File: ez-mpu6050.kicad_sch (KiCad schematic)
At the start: 25 parts, among them J1 I2C, J3 Conn_01x06, J4 Conn_01x06, J5 I2C, U1 MPU-6050, U2 AP2112K-3.3

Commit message: Finish tracks add zone & GND vias
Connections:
- net +3V3: now also J4.2 (Pin_2); no longer J3.2 (Pin_2)
- net AD0: now also J3.1 (Pin_1); no longer J4.1 (Pin_1)
- net CLKIN: now also J3.5 (Pin_5); no longer J4.5 (Pin_5)
- net FSYNC_IN: now also J3.2 (Pin_2); no longer J4.2 (Pin_2)
- net GND: now also J3.6 (Pin_6), J4.3 (Pin_3); no longer J3.3 (Pin_3), J4.6 (Pin_6)
- net INT: now also J4.6 (Pin_6); no longer J3.6 (Pin_6)
- net SCL: now also J4.4 (Pin_4); no longer J3.4 (Pin_4)
- net SCL_EXT: now also J3.3 (Pin_3); no longer J4.3 (Pin_3)
- net SDA: now also J4.5 (Pin_5); no longer J3.5 (Pin_5)
- net SDA_EXT: now also J3.4 (Pin_4); no longer J4.4 (Pin_4)
- net VDD: now also J4.1 (Pin_1); no longer J3.1 (Pin_1)
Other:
- moved on the sheet: J3, J4
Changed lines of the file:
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@@
     )
   )
-  (symbol (lib_id "Connector_Generic:Conn_01x06") (at 33.02 85.09 0) (mirror y) (unit 1)
+  (symbol (lib_id "Connector_Generic:Conn_01x06") (at 33.02 114.3 0) (mirror y) (unit 1)
     (in_bom yes) (on_board yes) (dnp no)
-    (property "Reference" "J3" (at 30.48 85.09 0)
-      (effects (font (size 1.27 1.27)) (justify left))
-    )
-    (property "Value" "Conn_01x06" (at 30.48 87.63 0)
-      (effects (font (size 1.27 1.27)) (justify left))
-    )
-    (property "Footprint" "Connector_PinHeader_2.54mm:PinHeader_1x06_P2.54mm_Vertical" (at 33.02 85.09 0)
-      (effects (font (size 1.27 1.27)) hide)
-    )
-    (property "Datasheet" "~" (at 33.02 85.09 0)
+    (property "Reference" "J3" (at 30.48 114.3 0)
+      (effects (font (size 1.27 1.27)) (justify left))
+    )
+    (property "Value" "Conn_01x06" (at 30.48 116.84 0)
+      (effects (font (size 1.27 1.27)) (justify left))
+    )
+    (property "Footprint" "Connector_PinHeader_2.54mm:PinHeader_1x06_P2.54mm_Vertical" (at 33.02 114.3 0)
+      (effects (font (size 1.27 1.27)) hide)
+    )
+    (property "Datasheet" "~" (at 33.02 114.3 0)
       (effects (font (size 1.27 1.27)) hide)
     )
@@
     )
   )
-  (symbol (lib_id "Connector_Generic:Conn_01x06") (at 33.02 114.3 0) (mirror y) (unit 1)
+  (symbol (lib_id "Connector_Generic:Conn_01x06") (at 33.02 85.09 0) (mirror y) (unit 1)
     (in_bom yes) (on_board yes) (dnp no)
-    (property "Reference" "J4" (at 30.48 114.3 0)
-      (effects (font (size 1.27 1.27)) (justify left))
-    )
-    (property "Value" "Conn_01x06" (at 30.48 116.84 0)
-      (effects (font (size 1.27 1.27)) (justify left))
-    )
-    (property "Footprint" "Connector_PinHeader_2.54mm:PinHeader_1x06_P2.54mm_Vertical" (at 33.02 114.3 0)
-      (effects (font (size 1.27 1.27)) hide)
-    )
-    (property "Datasheet" "~" (at 33.02 114.3 0)
-      (effects (font (size 1.27 1.27)) hide)
-    )
+    (property "Reference" "J4" (at 30.48 85.09 0)
+      (effects (font (size 1.27 1.27)) (justify left))
+    )
+    (property "Value" "Conn_01x06" (at 30.48 87.63 0)
+      (effects (font (size 1.27 1.27)) (justify left))
+    )
+    (property "Footprint" "Connector_PinHeader_2.54mm:PinHeader_1x06_P2.54mm_Vertical" (at 33.02 85.09 0)
+      (effects (font (size 1.27 1.27)) hide)
+    )
+    (property "Datasheet" "~" (at 33.02 85.09 0)
+      (effects (font (size 1.27 1.27)) hide)
+    )

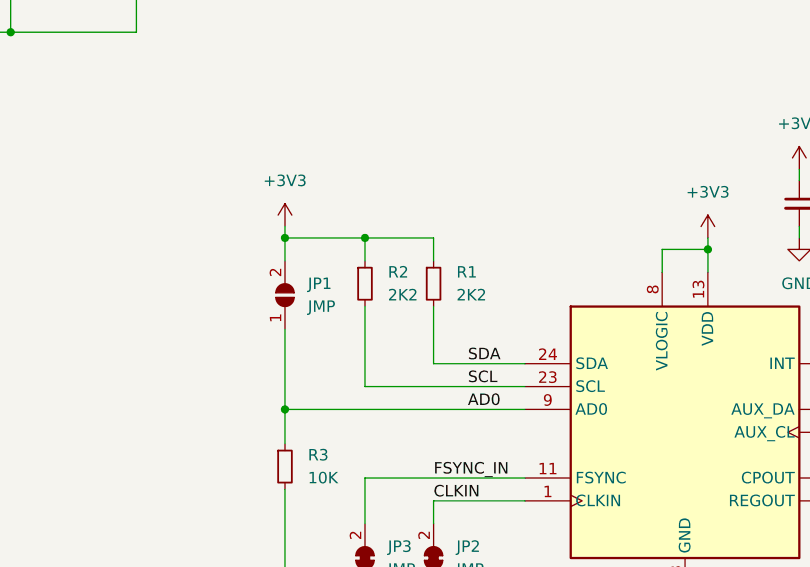
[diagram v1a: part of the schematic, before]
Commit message: Add RPU enable jumper
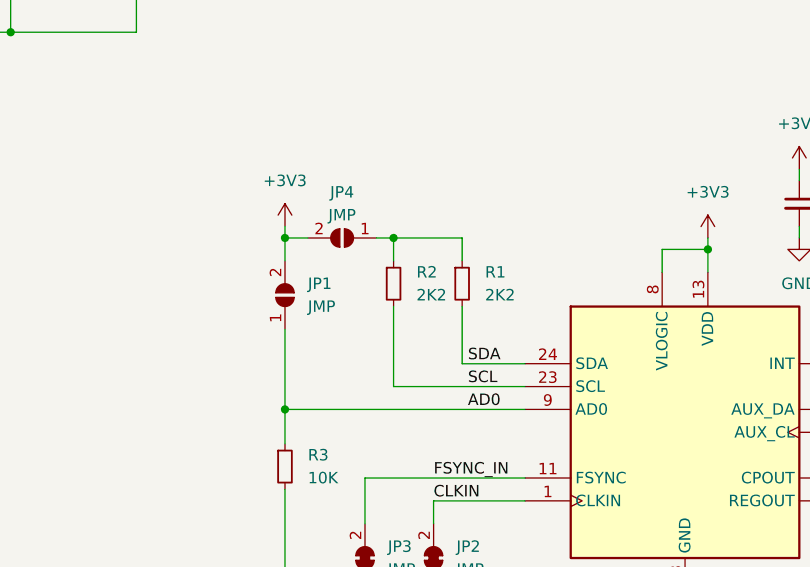
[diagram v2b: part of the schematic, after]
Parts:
- added JP4: JMP, Jumper:SolderJumper-2_P1.3mm_Open_RoundedPad1.0x1.5mm, symbol Jumper:SolderJumper_2_Open
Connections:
- net +3V3: now also JP4.2 (B); no longer R1.1, R2.1
- new net: JP4.1 (A), R1.1, R2.1
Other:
- moved on the sheet: R1, R2
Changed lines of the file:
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@@
   (junction (at 160.02 82.55) (diameter 0) (color 0 0 0 0)
   )
+  (junction (at 125.095 81.28) (diameter 0) (color 0 0 0 0)
+  )
   (junction (at 82.55 44.45) (diameter 0) (color 0 0 0 0)
   )
-  (junction (at 121.92 81.28) (diameter 0) (color 0 0 0 0)
-  )
   (junction (at 185.42 33.02) (diameter 0) (color 0 0 0 0)
   )
+  (junction (at 113.03 81.28) (diameter 0) (color 0 0 0 0)
+  )
   (junction (at 82.55 58.42) (diameter 0) (color 0 0 0 0)
   )
@@
   (junction (at 69.85 44.45) (diameter 0) (color 0 0 0 0)
   )
-  (junction (at 113.03 81.28) (diameter 0) (color 0 0 0 0)
-  )
   (junction (at 186.69 35.56) (diameter 0) (color 0 0 0 0)
   )
@@
     (stroke (width 0) (type default))
   )
-  (wire (pts (xy 121.92 97.79) (xy 139.7 97.79))
+  (wire (pts (xy 113.03 81.28) (xy 115.57 81.28))
+    (stroke (width 0) (type default))
+  )
+  (wire (pts (xy 125.095 97.79) (xy 139.7 97.79))
     (stroke (width 0) (type default))
   )
@@
     (stroke (width 0) (type default))
   )
-  (wire (pts (xy 121.92 81.28) (xy 129.54 81.28))
+  (wire (pts (xy 125.095 81.28) (xy 132.715 81.28))
     (stroke (width 0) (type default))
   )
@@
     (stroke (width 0) (type default))
   )
-  (wire (pts (xy 121.92 81.28) (xy 121.92 83.82))
+  (wire (pts (xy 125.095 81.28) (xy 125.095 83.82))
     (stroke (width 0) (type default))
   )
@@
     (stroke (width 0) (type default))
   )
+  (wire (pts (xy 113.03 81.28) (xy 113.03 83.82))
+    (stroke (width 0) (type default))
+  )
   (wire (pts (xy 154.94 85.09) (xy 154.94 82.55))
     (stroke (width 0) (type default))
@@
     (stroke (width 0) (type default))
   )
-  (wire (pts (xy 129.54 95.25) (xy 139.7 95.25))
+  (wire (pts (xy 132.715 95.25) (xy 139.7 95.25))
     (stroke (width 0) (type default))
   )
@@
     (stroke (width 0) (type default))
   )
-  (wire (pts (xy 113.03 81.28) (xy 121.92 81.28))
-    (stroke (width 0) (type default))
-  )
   (wire (pts (xy 38.1 119.38) (xy 48.26 119.38))
     (stroke (width 0) (type default))
@@
     (stroke (width 0) (type default))
   )
-  (wire (pts (xy 113.03 81.28) (xy 113.03 83.82))
-    (stroke (width 0) (type default))
-  )
   (wire (pts (xy 182.88 81.28) (xy 182.88 80.01))
     (stroke (width 0) (type default))
@@
     (stroke (width 0) (type default))
   )
-  (wire (pts (xy 129.54 88.9) (xy 129.54 95.25))
+  (wire (pts (xy 132.715 88.9) (xy 132.715 95.25))
     (stroke (width 0) (type default))
   )
@@
     (stroke (width 0) (type default))
   )
+  (wire (pts (xy 123.19 81.28) (xy 125.095 81.28))
+    (stroke (width 0) (type default))
+  )
   (wire (pts (xy 121.92 113.03) (xy 121.92 107.95))
     (stroke (width 0) (type default))
@@
     (stroke (width 0) (type default))
   )
-  (wire (pts (xy 121.92 88.9) (xy 121.92 97.79))
+  (wire (pts (xy 125.095 88.9) (xy 125.095 97.79))
     (stroke (width 0) (type default))
   )
@@
     (stroke (width 0) (type default))
   )
-  (wire (pts (xy 129.54 83.82) (xy 129.54 81.28))
+  (wire (pts (xy 132.715 83.82) (xy 132.715 81.28))
     (stroke (width 0) (type default))
   )
@@
       (effects (font (size 1.27 1.27)) hide)
     )
-    (pin "2")
-    (pin "1")
+    (pin "1")
+    (pin "2")
     (instances
       (project "ez-mpu6050"
@@
       (effects (font (size 1.27 1.27)) (justify bottom) hide)
     )
-    (pin "2")
+    (pin "1")
+    (pin "2")
+    (pin "3")
     (pin "4")
-    (pin "1")
     (pin "S1")
     (pin "S2")
-    (pin "3")
     (instances
       (project "ez-mpu6050"
@@
       (effects (font (size 1.27 1.27)) hide)
     )
-    (pin "6")
     (pin "1")
     (pin "2")
@@
     (pin "4")
     (pin "5")
+    (pin "6")
     (instances
       (project "ez-mpu6050"
@@
     )
   )
-  (symbol (lib_id "Device:R_Small") (at 129.54 86.36 0) (unit 1)
-    (in_bom yes) (on_board yes) (dnp no) (fields_autoplaced)
-    (property "Reference" "R1" (at 132.08 85.09 0)
-      (effects (font (size 1.27 1.27)) (justify left))
-    )
-    (property "Value" "2K2" (at 132.08 87.63 0)
-      (effects (font (size 1.27 1.27)) (justify left))
-    )
-    (property "Footprint" "Resistor_SMD:R_0402_1005Metric" (at 129.54 86.36 0)
-      (effects (font (size 1.27 1.27)) hide)
-    )
-    (property "Datasheet" "~" (at 129.54 86.36 0)
-      (effects (font (size 1.27 1.27)) hide)
-    )
-    (pin "2")
-    (pin "1")
+  (symbol (lib_id "Device:R_Small") (at 132.715 86.36 0) (unit 1)
+    (in_bom yes) (on_board yes) (dnp no) (fields_autoplaced)
+    (property "Reference" "R1" (at 135.255 85.09 0)
+      (effects (font (size 1.27 1.27)) (justify left))
+    )
+    (property "Value" "2K2" (at 135.255 87.63 0)
+      (effects (font (size 1.27 1.27)) (justify left))
+    )
+    (property "Footprint" "Resistor_SMD:R_0402_1005Metric" (at 132.715 86.36 0)
+      (effects (font (size 1.27 1.27)) hide)
+    )
+    (property "Datasheet" "~" (at 132.715 86.36 0)
+      (effects (font (size 1.27 1.27)) hide)
+    )
+    (pin "1")
+    (pin "2")
     (instances
       (project "ez-mpu6050"
@@
     )
     (pin "1")
+    (pin "2")
     (pin "3")
     (pin "4")
     (pin "5")
-    (pin "2")
     (instances
       (project "ez-mpu6050"
@@
     )
   )
-  (symbol (lib_id "Device:R_Small") (at 121.92 86.36 0) (unit 1)
-    (in_bom yes) (on_board yes) (dnp no) (fields_autoplaced)
-    (property "Reference" "R2" (at 124.46 85.09 0)
-      (effects (font (size 1.27 1.27)) (justify left))
-    )
-    (property "Value" "2K2" (at 124.46 87.63 0)
-      (effects (font (size 1.27 1.27)) (justify left))
-    )
-    (property "Footprint" "Resistor_SMD:R_0402_1005Metric" (at 121.92 86.36 0)
-      (effects (font (size 1.27 1.27)) hide)
-    )
-    (property "Datasheet" "~" (at 121.92 86.36 0)
-      (effects (font (size 1.27 1.27)) hide)
-    )
-    (pin "2")
-    (pin "1")
+  (symbol (lib_id "Device:R_Small") (at 125.095 86.36 0) (unit 1)
+    (in_bom yes) (on_board yes) (dnp no) (fields_autoplaced)
+    (property "Reference" "R2" (at 127.635 85.09 0)
+      (effects (font (size 1.27 1.27)) (justify left))
+    )
+    (property "Value" "2K2" (at 127.635 87.63 0)
+      (effects (font (size 1.27 1.27)) (justify left))
+    )
+    (property "Footprint" "Resistor_SMD:R_0402_1005Metric" (at 125.095 86.36 0)
+      (effects (font (size 1.27 1.27)) hide)
+    )
+    (property "Datasheet" "~" (at 125.095 86.36 0)
+      (effects (font (size 1.27 1.27)) hide)
+    )
+    (pin "1")
+    (pin "2")
     (instances
       (project "ez-mpu6050"
@@
       (effects (font (size 1.27 1.27)) (justify bottom) hide)
     )
-    (pin "2")
+    (pin "1")
+    (pin "2")
+    (pin "3")
     (pin "4")
-    (pin "1")
     (pin "S1")
     (pin "S2")
-    (pin "3")
     (instances
       (project "ez-mpu6050"
         (path "/337b384b-6392-4926-8df2-8308a7b00af3"
           (reference "J5") (unit 1)
+        )
+      )
+    )
+  )
+  (symbol (lib_id "Jumper:SolderJumper_2_Open") (at 119.38 81.28 180) (unit 1)
+    (in_bom yes) (on_board yes) (dnp no) (fields_autoplaced)
+    (property "Reference" "JP4" (at 119.38 76.2 0)
+      (effects (font (size 1.27 1.27)))
+    )
+    (property "Value" "JMP" (at 119.38 78.74 0)
+      (effects (font (size 1.27 1.27)))
+    )
+    (property "Footprint" "Jumper:SolderJumper-2_P1.3mm_Open_RoundedPad1.0x1.5mm" (at 119.38 81.28 0)
+      (effects (font (size 1.27 1.27)) hide)
+    )
+    (property "Datasheet" "~" (at 119.38 81.28 0)
+      (effects (font (size 1.27 1.27)) hide)
+    )
+    (pin "1")
+    (pin "2")
+    (instances
+      (project "ez-mpu6050"
+        (path "/337b384b-6392-4926-8df2-8308a7b00af3"
+          (reference "JP4") (unit 1)
         )
       )
@@
       (effects (font (size 1.27 1.27)) hide)
     )
-    (pin "2")
-    (pin "1")
+    (pin "1")
+    (pin "2")
     (instances
       (project "ez-mpu6050"
@@
       (effects (font (size 1.27 1.27)) hide)
     )
-    (pin "2")
-    (pin "1")
+    (pin "1")
+    (pin "2")
     (instances
       (project "ez-mpu6050"
@@
       (effects (font (size 1.27 1.27)) hide)
     )
-    (pin "2")
-    (pin "1")
+    (pin "1")
+    (pin "2")
     (instances
       (project "ez-mpu6050"
@@
       (effects (font (size 1.27 1.27)) hide)
     )
-    (pin "6")
     (pin "1")
     (pin "2")
@@
     (pin "4")
     (pin "5")
+    (pin "6")
     (instances
       (project "ez-mpu6050"
@@
       (effects (font (size 1.27 1.27)) hide)
     )
-    (pin "2")
-    (pin "1")
+    (pin "1")
+    (pin "2")
     (instances
       (project "ez-mpu6050"
@@
       (effects (font (size 1.27 1.27)) hide)
     )
-    (pin "9")
+    (pin "1")
+    (pin "10")
+    (pin "11")
+    (pin "12")
+    (pin "13")
+    (pin "14")
+    (pin "15")
+    (pin "16")
+    (pin "17")
+    (pin "18")
+    (pin "19")
+    (pin "2")
+    (pin "20")
     (pin "21")
     (pin "22")
-    (pin "19")
     (pin "23")
-    (pin "14")
-    (pin "1")
-    (pin "18")
-    (pin "16")
-    (pin "8")
-    (pin "5")
-    (pin "17")
-    (pin "2")
-    (pin "20")
+    (pin "24")
     (pin "3")
     (pin "4")
-    (pin "12")
+    (pin "5")
+    (pin "6")
     (pin "7")
-    (pin "6")
-    (pin "24")
-    (pin "15")
-    (pin "13")
-    (pin "11")
-    (pin "10")
+    (pin "8")
+    (pin "9")
     (instances
       (project "ez-mpu6050"
@@
       (effects (font (size 1.27 1.27)) hide)
     )
-    (pin "2")
-    (pin "1")
+    (pin "1")
+    (pin "2")
     (instances
       (project "ez-mpu6050"
@@
       (effects (font (size 1.27 1.27)) hide)
     )
-    (pin "2")
-    (pin "1")
-    (instances
-      (project "ez-mpu6050"
+    (pin "1")
+    (pin "2")
+    (instances
+      (project "ez-mpu6050"
